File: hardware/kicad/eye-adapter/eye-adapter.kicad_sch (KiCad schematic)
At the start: 9 parts, among them J11 vom Mainboard J7, J12 GC9A01 links, J13 GC9A01 rechts

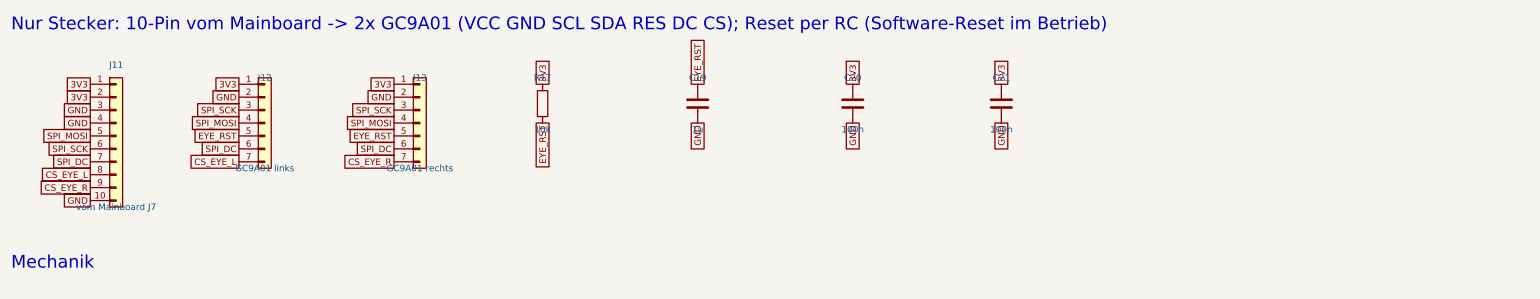
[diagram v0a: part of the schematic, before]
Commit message: Session 2026-10-03 00:27: Reserve raus (Stepper, C3, GPIO45, 7 Loetjumper), alle drei Platinen neu geroutet; Push und Falle 18 behoben
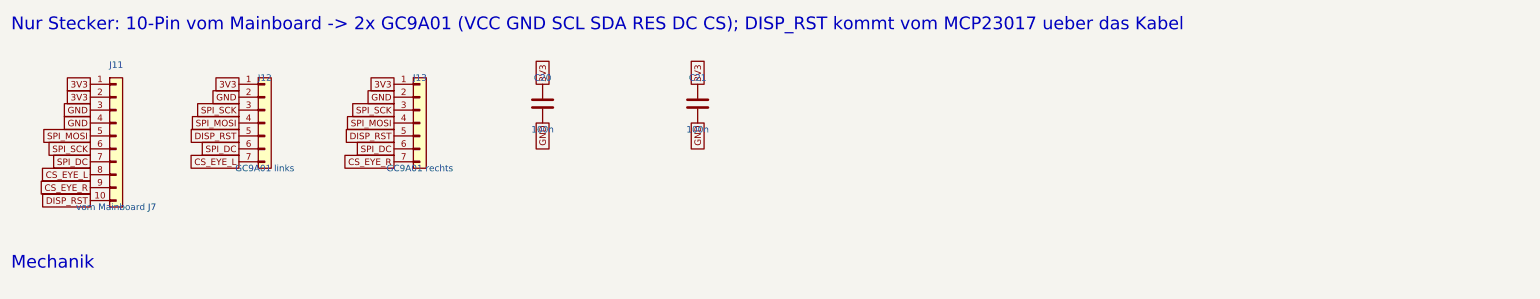
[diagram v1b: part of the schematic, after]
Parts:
- removed C19: 1u, Capacitor_THT:C_Disc_D5.0mm_W2.5mm_P5.00mm, symbol Device:C
- removed R17: 10k, Resistor_THT:R_Axial_DIN0207_L6.3mm_D2.5mm_P7.62mm_Horizontal, symbol Device:R
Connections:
- net GND: no longer J11.10 (Pin_10)
- net EYE_RST renamed DISP_RST
- net DISP_RST: now also J11.10 (Pin_10)
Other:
- note added: "Nur Stecker: 10-Pin vom Mainboard -> 2x GC9A01 (VCC GND SCL SDA RES DC CS); DISP_RST kommt vom MCP23017 ueber das Kabel"
- note removed: "Nur Stecker: 10-Pin vom Mainboard -> 2x GC9A01 (VCC GND SCL SDA RES DC CS); Reset per RC (Software-Reset im Betrieb)"
- moved on the sheet: C20, C21

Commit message: Session 2026-10-09 11:37: Platinen finalisiert: Teile von Reichelt, Silkscreen mit Logo und Pin-Namen, alle drei Boards neu geroutet
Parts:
- J11: value vom Mainboard J7 -> IDC 2x5 vom Mainboard J7; footprint Connector_PinHeader_2.54mm:PinHeader_1x10_P2.54mm_Vertical -> Connector_IDC:IDC-Header_2x05_P2.54mm_Vertical; symbol Connector_Generic:Conn_01x10 -> Connector_Generic:Conn_02x05_Odd_Even
- J12: value GC9A01 links -> GC9A01 links (Dupont); footprint Connector_PinSocket_2.54mm:PinSocket_1x07_P2.54mm_Vertical -> Connector_PinHeader_2.54mm:PinHeader_1x07_P2.54mm_Vertical
- J13: value GC9A01 rechts -> GC9A01 rechts (Dupont); footprint Connector_PinSocket_2.54mm:PinSocket_1x07_P2.54mm_Vertical -> Connector_PinHeader_2.54mm:PinHeader_1x07_P2.54mm_Vertical
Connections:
- net 3V3: no longer J11.2 (Pin_2)
- net GND: now also J11.2 (Pin_2), J11.6 (Pin_6); no longer J11.3 (Pin_3)
- net SPI_SCK: now also J11.3 (Pin_3); no longer J11.6 (Pin_6)
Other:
- note added: "Nur Stecker: IDC 2x5 vom Mainboard -> 2x 1x7-Stiftleiste in GC9A01-Reihenfolge (VCC GND SCL SDA RES DC CS), Displays per Dupont-Kabel; DISP_RST kommt vom MCP23017"
- note removed: "Nur Stecker: 10-Pin vom Mainboard -> 2x GC9A01 (VCC GND SCL SDA RES DC CS); DISP_RST kommt vom MCP23017 ueber das Kabel"
- moved on the sheet: C20, C21, H13, H14, J11, J12, J13
